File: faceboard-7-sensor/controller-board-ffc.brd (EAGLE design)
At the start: 52 x 66 mm, 13 parts

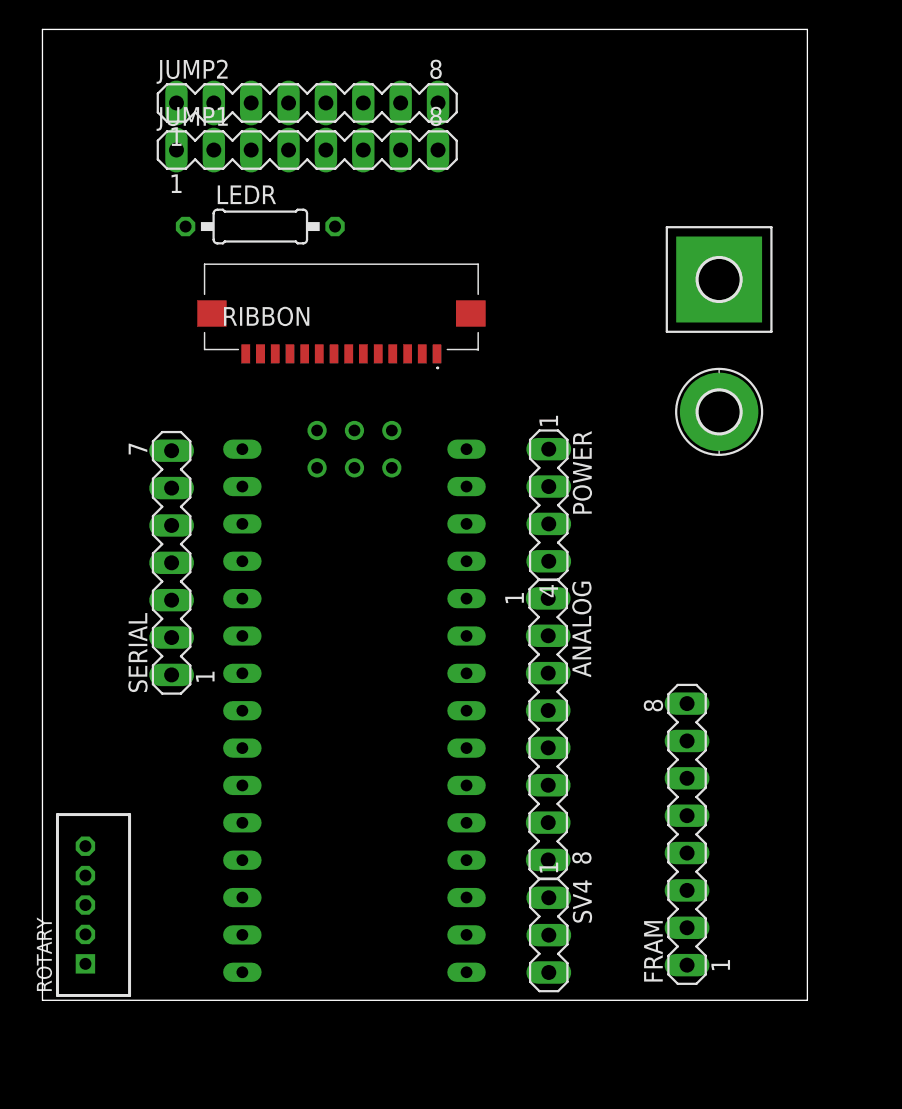
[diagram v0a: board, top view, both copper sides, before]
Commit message: add ffc boards
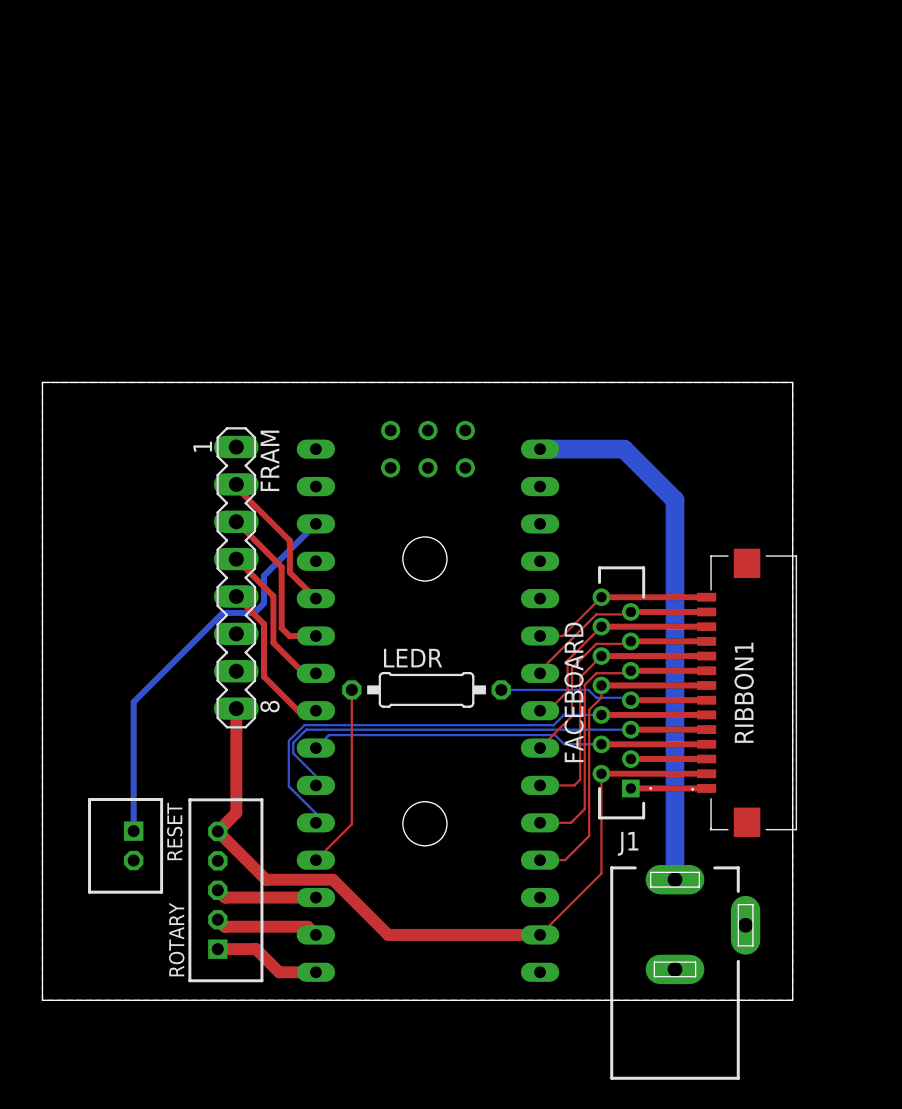
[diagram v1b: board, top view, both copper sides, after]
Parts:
- removed ANALOG: SIGNALS, con-lstb:MA08-1
- removed H1: MOUNT-PAD-ROUND2.8, holes:2,8-PAD
- removed H2: MOUNT-PAD-SQUARE2.8, holes:2,8-PAD-SQUARE
- removed JUMP1, JUMP2: HEADER, con-lstb:MA08-1
- removed POWER: POWER, con-lstb:MA04-1
- removed RIBBON: 686114148922, 686114148922:686114148922
- removed SERIAL: ARDUINO4, con-lstb:MA07-1
- removed SV4: J3, con-lstb:MA03-1
- added FACEBOARD: 52806-1410, 52806-1410:528061410
- added J1: DCJ0202, con-jack:DCJ0202
- added RESET: B2B-PH-K, con-jst-ph:B2B-PH-K
- added RIBBON1: 686114148922, 686114148922:686114148922
- FRAM: value FRAM -> MB85RS2MTA
- moved FRAM 35.3 mm to (13.2, 28.7), turned to 270 degrees
- moved LEDR 33.5 mm to (26.1, 21.1)
- moved ROTARY 9.06 mm to (11.9, 7.48)
- moved U$1 5.00 mm to (23.7, 28.6)
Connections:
- removed net 3.3V: SV4.2, U$1.3.3V
- removed net N$3: FRAM.6
- new net NC3V: FRAM.7
- new net RST0: U$1.RST
- net 3V: now also FACEBOARD.2, RIBBON1.2, U$1.3.3V; no longer RIBBON.13
- net 5V: now also FACEBOARD.3, RIBBON1.3; no longer RIBBON.12
- net A: now also FACEBOARD.4, RIBBON1.4; no longer RIBBON.11
- net A0: now also FACEBOARD.8, RIBBON1.8; no longer ANALOG.8, RIBBON.1
- net A1: now also FACEBOARD.9, RIBBON1.9; no longer ANALOG.7, RIBBON.2
- net A2: now also FACEBOARD.10, RIBBON1.10; no longer ANALOG.6, RIBBON.3
- net A3: now also FACEBOARD.11, RIBBON1.11; no longer ANALOG.5, RIBBON.4
- net A4: now also FACEBOARD.12, RIBBON1.12; no longer ANALOG.4, RIBBON.5
- net A5: now also FACEBOARD.13, RIBBON1.13; no longer ANALOG.3, RIBBON.6
- net A6: now also FACEBOARD.14, RIBBON1.14; no longer ANALOG.2, RIBBON.7
- net A7: no longer ANALOG.1
- net AREF: no longer SV4.1
- net B: now also FACEBOARD.5, RIBBON1.5; no longer RIBBON.10
- net C: now also FACEBOARD.6, RIBBON1.6; no longer RIBBON.9
- net D0: no longer SERIAL.7
- net D1: no longer SERIAL.6
- net D13: no longer SV4.3
- net FRAM_CS: no longer SERIAL.3
- net FRAM_MOSI: no longer SERIAL.2
- net GND: now also FACEBOARD.1, FRAM.6, J1.2, J1.3, RESET.2, RIBBON1.1, RIBBON1.MP1, RIBBON1.MP2; no longer FRAM.7, H2.B2,8, POWER.2, RIBBON.14, RIBBON.MP1, RIBBON.MP2, SERIAL.4
- net LEDDATA: now also FACEBOARD.7, RIBBON1.7; no longer RIBBON.8
- net RST: now also RESET.1; no longer POWER.3, SERIAL.5, U$1.RST
- net VIN: now also J1.1; no longer H1.B2,8, POWER.1
- net VUSB: no longer POWER.4
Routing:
- net 3V: track 0.00 -> 53.5 mm
- net VIN: track 0.00 -> 36.4 mm
- net C: track 0.00 -> 35.5 mm
- net B: track 0.00 -> 32.0 mm
- net RST: track 0.00 -> 27.3 mm
- net A: track 0.00 -> 27.2 mm
- net A0: track 0.00 -> 21.7 mm
- net A1: track 0.00 -> 20.5 mm
- net A2: track 0.00 -> 19.0 mm
- net A3: track 0.00 -> 16.2 mm
- net A4: track 0.00 -> 14.9 mm
- net LEDDATA: track 0.00 -> 14.2 mm
- net A5: track 0.00 -> 13.2 mm
- net D9: track 0.00 -> 12.6 mm
- net A6: track 0.00 -> 12.4 mm
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- added copper zone on layer 1, net GND
- added copper zone on layer 16, net GND
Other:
- board size 52 x 66 mm -> 51 x 42 mm
- board text added: "NEMUS Controller Board v0.1.2"

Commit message: tidy routing
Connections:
- removed net VIN: J1.1, U$1.RAW
- net 5V: now also J1.1, U$1.RAW
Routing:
- net 5V: track 5.15 -> 44.7 mm
- net VIN: track 36.4 -> 0.00 mm
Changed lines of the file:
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@@
 <wire x1="12.25986875" y1="26.3324" x2="14.40493125" y2="26.3324" width="0.4064" layer="16"/>
-</signal>
-<signal name="VIN">
-<contactref element="U$1" pad="RAW"/>
-<contactref element="J1" pad="1"/>
-<wire x1="43" y1="8.2" x2="43" y2="34" width="1.27" layer="16"/>
-<wire x1="43" y1="34" x2="39.535" y2="37.465" width="1.27" layer="16"/>
-<wire x1="39.535" y1="37.465" x2="33.829" y2="37.465" width="1.27" layer="16"/>
 </signal>
 <signal name="GND">
@@
 <contactref element="FACEBOARD" pad="3"/>
 <wire x1="45.15" y1="16.4" x2="40" y2="16.4" width="0.4064" layer="1"/>
+<contactref element="U$1" pad="RAW"/>
+<contactref element="J1" pad="1"/>
+<wire x1="43" y1="8.2" x2="43" y2="16" width="1.27" layer="16"/>
+<wire x1="43" y1="16" x2="43" y2="34" width="1.27" layer="16"/>
+<wire x1="43" y1="34" x2="39.535" y2="37.465" width="1.27" layer="16"/>
+<wire x1="39.535" y1="37.465" x2="33.829" y2="37.465" width="1.27" layer="16"/>
+<wire x1="43" y1="16" x2="40.4" y2="16" width="0.4064" layer="16"/>
+<wire x1="40.4" y1="16" x2="40" y2="16.4" width="0.4064" layer="16"/>
 </signal>
 <signal name="3V">

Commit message: redraw schematics
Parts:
- removed FACEBOARD: 52806-1410, 52806-1410:528061410
- RIBBON1: value 686114148922 -> (none)
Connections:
- net FRAM_CLK renamed CLK
- net FRAM_CS renamed CS
- net FRAM_MISO renamed MISO
- net FRAM_MOSI renamed MOSI
- net ROTA renamed RA
- net ROTB renamed RB
- net ROTC renamed RC
- removed net 5V: FACEBOARD.3, J1.1, RIBBON1.3, U$1.RAW
- removed net A4: FACEBOARD.12, RIBBON1.12, U$1.A4
- removed net A6: FACEBOARD.14, RIBBON1.14, U$1.A6
- removed net A7: U$1.A7
- removed net AREF: U$1.AREF
- removed net D0: U$1.TX0
- removed net D1: U$1.RX1
- removed net D13: U$1.D13
- removed net LEDDATA: FACEBOARD.7, LEDR.2, RIBBON1.7
- removed net N$8: FRAM.1
- removed net NC3V: FRAM.7
- removed net RST0: U$1.RST
- removed net VUSB: U$1.5V
- new net DIN: LEDR.2, RIBBON1.7
- new net N$1: RIBBON1.12, U$1.A4
- new net N$2: RIBBON1.14, U$1.A6
- new net VCC: J1.1, RIBBON1.3, U$1.RAW
- net 3V: no longer FACEBOARD.2
- net A: no longer FACEBOARD.4
- net A0: no longer FACEBOARD.8
- net A1: no longer FACEBOARD.9
- net A2: no longer FACEBOARD.10
- net A3: no longer FACEBOARD.11
- net A5: no longer FACEBOARD.13
- net B: no longer FACEBOARD.5
- net C: no longer FACEBOARD.6
- net GND: no longer FACEBOARD.1
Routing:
- net 5V: track 44.7 -> 0.00 mm
- net B: track 32.0 -> 4.80 mm
- net A4: track 14.9 -> 0.00 mm
- net LEDDATA: track 14.2 -> 0.00 mm
- net 3V: track 53.5 -> 39.6 mm
- net A6: track 12.4 -> 0.00 mm
- net C: track 35.5 -> 25.8 mm
- net A: track 27.2 -> 17.5 mm
- net A2: track 19.0 -> 9.85 mm
- net DIN: track 0.00 -> 8.86 mm
- net A0: track 21.7 -> 13.8 mm
- net RA: track 6.87 -> 0.70 mm
- net A1: track 20.5 -> 15.2 mm
- net A5: track 13.2 -> 7.77 mm
- net A3: track 16.2 -> 10.8 mm
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
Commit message: reroute
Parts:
- RIBBON1: value (none) -> Signal
- moved J1 30.0 mm to (45.9, 35.0), turned to 90 degrees
- moved RIBBON1 2.83 mm to (46.2, 18.9)
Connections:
- net N$1 renamed A4
- net N$2 renamed A6
- net A: now also U$1.D8; no longer U$1.D6
- net C: now also U$1.D6; no longer U$1.D8
- net GND: now also FRAM.7; no longer FRAM.6
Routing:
- net VCC: track 0.00 -> 34.1 mm
- net B: track 4.80 -> 29.8 mm, vias 0 -> 1
- net A: track 17.5 -> 29.0 mm, vias 0 -> 1
- net A4: track 0.00 -> 10.9 mm
- net DIN: track 8.86 -> 18.8 mm, vias 0 -> 1
- net A6: track 0.00 -> 9.58 mm
- net 3V: track 39.6 -> 47.0 mm
- net RA: track 0.70 -> 6.87 mm
- net RC: track 4.83 -> 7.32 mm
- net D9: track 12.6 -> 15.0 mm
- net A5: track 7.77 -> 10.2 mm
- net A1: track 15.2 -> 12.8 mm
- net A2: track 9.85 -> 12.1 mm
- net C: track 25.8 -> 27.7 mm, vias 0 -> 1
- net RB: track 6.31 -> 7.10 mm
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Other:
- board text added: "NEMUS Controller Board v0.1.3"
- board text removed: "NEMUS Controller Board v0.1.2"
